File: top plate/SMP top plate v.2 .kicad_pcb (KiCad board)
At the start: 2 copper layers, 123.8 x 58.7 mm, 4 parts

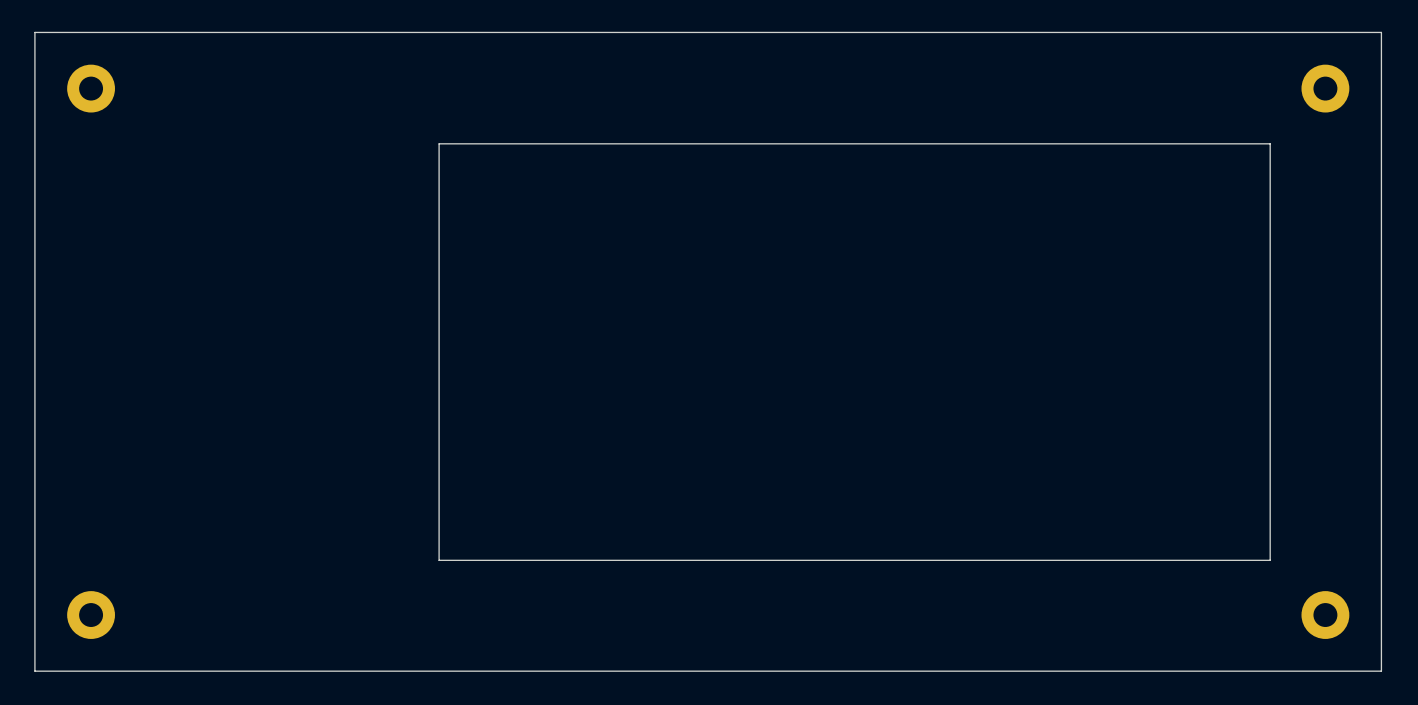
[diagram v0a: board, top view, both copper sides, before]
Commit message: fine tune top plate after prototype 1
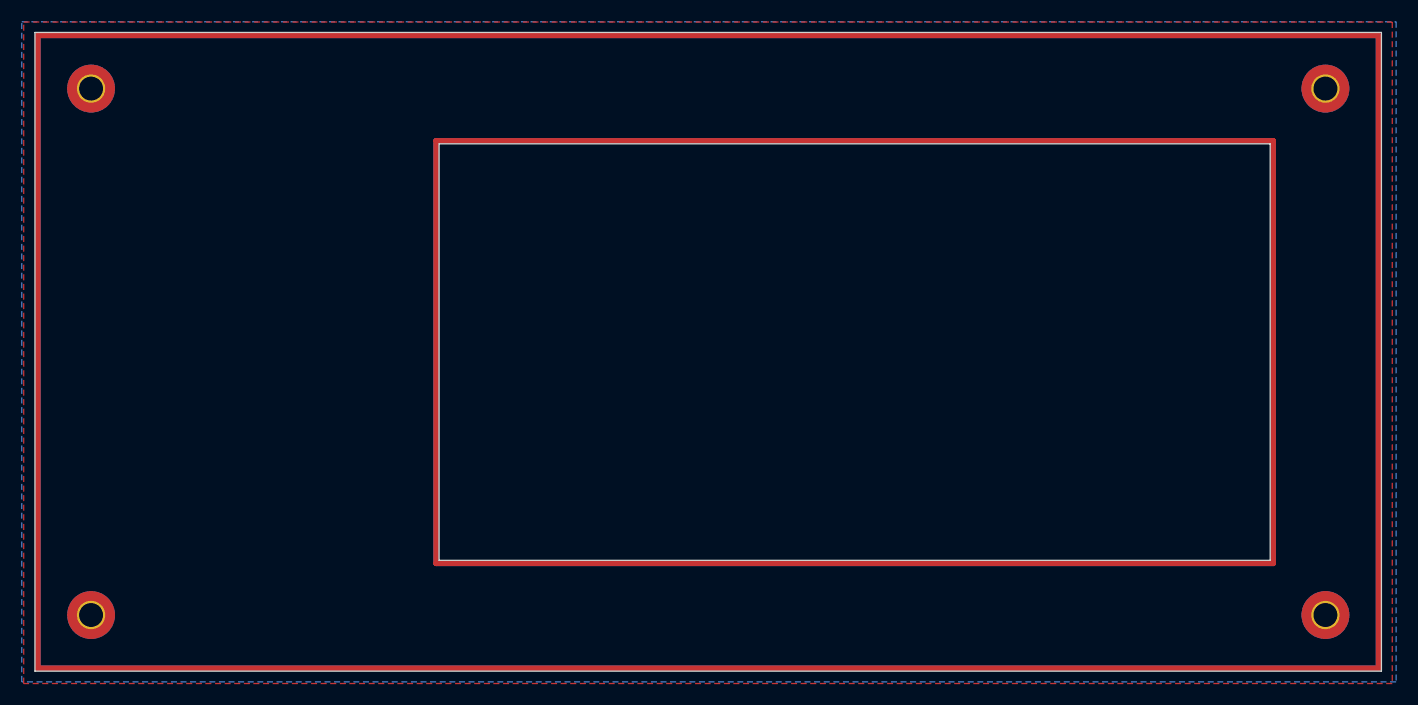
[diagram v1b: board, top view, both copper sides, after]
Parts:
- removed ? (x3), REF**: MountingHole_2.2mm_M2_Pad, MountingHole:MountingHole_2.2mm_M2_Pad
- added H1: MountingHole_Pad, MountingHole:MountingHole_2.2mm_M2_Pad_TopBottom, F.Cu at (75.5, 76.4)
- added H2: MountingHole_Pad, MountingHole:MountingHole_2.2mm_M2_Pad_TopBottom, F.Cu at (75.5, 124.8)
- added H3: MountingHole_Pad, MountingHole:MountingHole_2.2mm_M2_Pad_TopBottom, F.Cu at (189.1, 76.4)
- added H4: MountingHole_Pad, MountingHole:MountingHole_2.2mm_M2_Pad_TopBottom, F.Cu at (189.1, 124.8)
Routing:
- added copper zone on B.Cu, net GND
- added copper zone on F.Cu, net GND
